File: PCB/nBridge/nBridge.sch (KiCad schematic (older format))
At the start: 23 parts, among them J1 USB_C_Receptacle_USB2.0, J2 Conn_01x06, J3 Conn_01x02, SW1 Switch-SPDT, U1 TPS7A0533PYKAR, U2 BQ25100YFPR, U3 BL652, U4 CC2500Module, U5 M41T62_LC

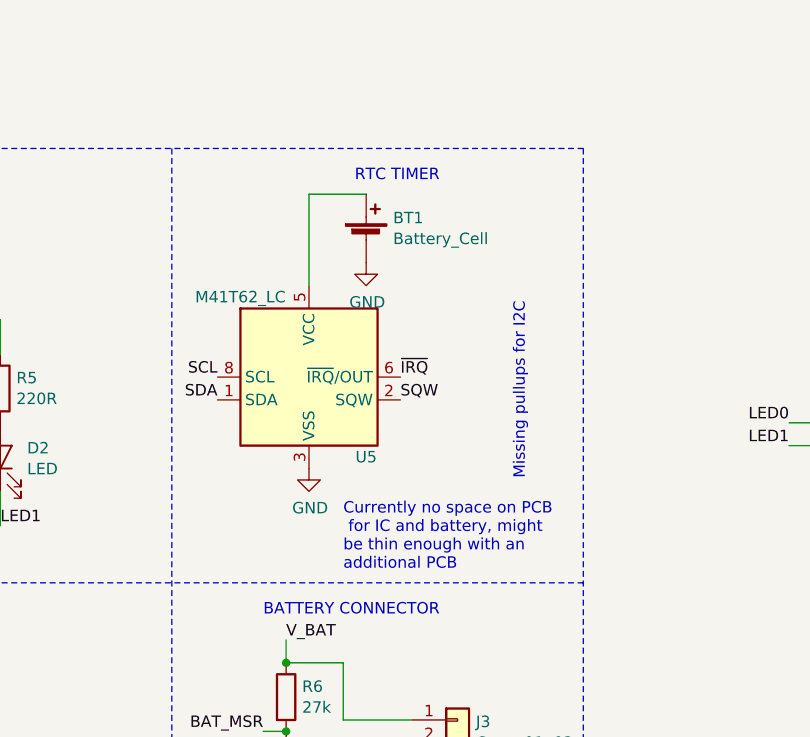
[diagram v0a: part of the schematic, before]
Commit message: Remove RTC
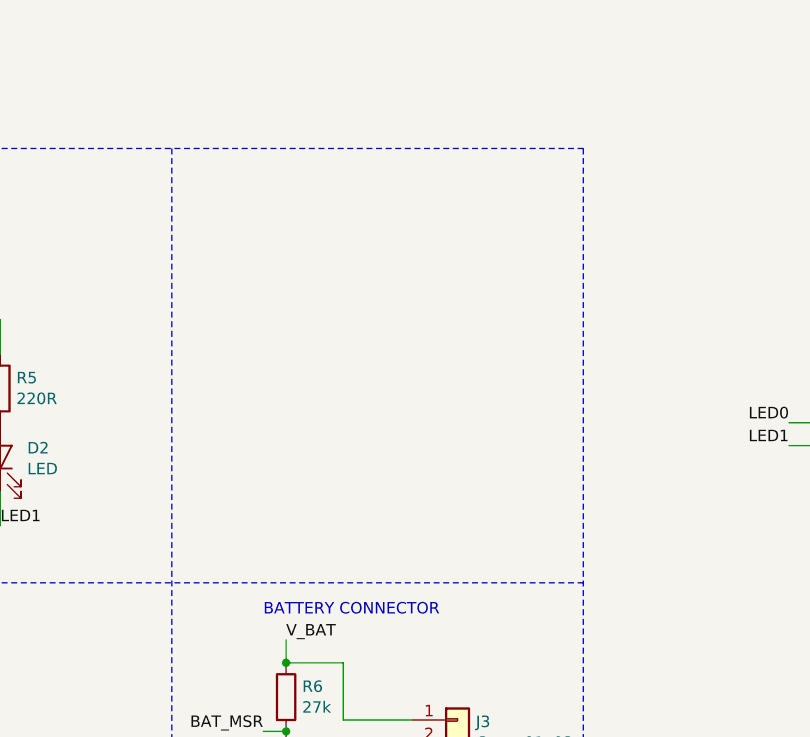
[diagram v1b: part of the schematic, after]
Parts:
- removed BT1: Battery_Cell, symbol Device:Battery_Cell
- removed U5: M41T62_LC, SharedFootprints:M41T62_LLC8_15x32, symbol SharedSymbols:M41T62_LC
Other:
- note removed: "Currently no space on PCB\n for IC and battery, might \nbe thin enough with an \nadditional PCB"
- note removed: "Missing pullups for I2C"
- note removed: "RTC TIMER"
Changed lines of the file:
@@
 Text Notes 1650 1000 0    50   ~ 0
 CC2500 MODULE
-$Comp
-L SharedSymbols:M41T62_LC U5
-U 1 1 5CB38CAA
-P 5750 4150
-F 0 "U5" H 6000 3800 50  0000 C CNN
-F 1 "M41T62_LC" H 5450 4500 50  0000 C CNN
-F 2 "SharedFootprints:M41T62_LLC8_15x32" H 5750 3450 50  0001 C CNN
-F 3 "http://www.st.com/resource/en/datasheet/m41t62.pdf" H 5750 4150 50  0001 C CNN
-	1    5750 4150
-	1    0    0    -1
-$EndComp
-Text Notes 5950 3300 0    50   ~ 0
-RTC TIMER
-$Comp
-L power:GND #PWR017
-U 1 1 5CB3C6E6
-P 5750 4550
-F 0 "#PWR017" H 5750 4300 50  0001 C CNN
-F 1 "GND" H 5755 4377 50  0000 C CNN
-F 2 "" H 5750 4550 50  0001 C CNN
-F 3 "" H 5750 4550 50  0001 C CNN
-	1    5750 4550
-	1    0    0    -1
-$EndComp
-Wire Wire Line
-	5750 3750 5750 3350
-Wire Wire Line
-	5750 3350 6000 3350
-$Comp
-L Device:Battery_Cell BT1
-U 1 1 5CB3FA69
-P 6000 3550
-F 0 "BT1" H 6118 3646 50  0000 L CNN
-F 1 "Battery_Cell" H 6118 3555 50  0000 L CNN
-F 2 "" V 6000 3610 50  0001 C CNN
-F 3 "~" V 6000 3610 50  0001 C CNN
-	1    6000 3550
-	1    0    0    -1
-$EndComp
-$Comp
-L power:GND #PWR018
-U 1 1 5CB4019A
-P 6000 3650
-F 0 "#PWR018" H 6000 3400 50  0001 C CNN
-F 1 "GND" H 6005 3477 50  0000 C CNN
-F 2 "" H 6000 3650 50  0001 C CNN
-F 3 "" H 6000 3650 50  0001 C CNN
-	1    6000 3650
-	1    0    0    -1
-$EndComp
-Text Label 5350 4150 2    50   ~ 0
-SCL
-Text Label 5350 4250 2    50   ~ 0
-SDA
-Text Label 6150 4250 0    50   ~ 0
-SQW
-Text Label 6150 4150 0    50   ~ 0
-~IRQ
-Text Notes 5900 5000 0    50   ~ 0
-Currently no space on PCB\n for IC and battery, might \nbe thin enough with an \nadditional PCB
-Text Notes 6700 4600 1    50   ~ 0
-Missing pullups for I2C
 $EndSCHEMATC

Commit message: Simplify design, fewer and more easily solderable components
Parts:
- removed J1: USB_C_Receptacle_USB2.0, SharedFootprints:12401610E4#2A, symbol Connector:USB_C_Receptacle_USB2.0
- removed R2: 1k35, Resistor_SMD:R_0402_1005Metric, symbol Device:R
- removed R3: 6k, Resistor_SMD:R_0402_1005Metric, symbol Device:R
- removed U1: TPS7A0533PYKAR, SharedFootprints:TPS7A0533PYKAR, symbol SharedSymbols:TPS7A0533PYKAR
- removed U2: BQ25100YFPR, SharedFootprints:BQ25100YFPR, symbol SharedSymbols:BQ25100YFPR
- added J1: 0473460001, digikey-footprints:USB_Micro_B_Female_0473460001, symbol dk_USB-DVI-HDMI-Connectors:0473460001
- added U1: LP5907MFX-3_3_NOPB, digikey-footprints:SOT-753, symbol dk_PMIC-Voltage-Regulators-Linear:LP5907MFX-3_3_NOPB
- added U2: MCP73812T-420I_OT, digikey-footprints:SOT-753, symbol dk_PMIC-Battery-Chargers:MCP73812T-420I_OT
- C1, C2, C3, C4: footprint Capacitor_SMD:C_0402_1005Metric -> Capacitor_SMD:C_0805_2012Metric
- R1: value 10k -> R; footprint Resistor_SMD:R_0402_1005Metric -> Resistor_SMD:R_0805_2012Metric
- R4, R5, R6, R7: footprint Resistor_SMD:R_0402_1005Metric -> Resistor_SMD:R_0805_2012Metric
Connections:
- net +3V3: now also U1.5 (OUT)
- net GND: now also SW1.1 (A), J1.5, J1.SH, U1.2 (GND), U2.2 (VSS); no longer SW1.2 (C)
- net LED0: now also D2.1 (K); no longer D1.1 (K)
- net LED1: now also D1.1 (K); no longer D2.1 (K)
- net V_BAT: now also SW1.2 (C), U1.1 (IN), U2.3 (VBAT); no longer SW1.1 (A)
- net USB+: now reaches C2.1
- net USB+: now also J1.1, U2.1 (CE), U2.4 (VDD)
- net at R1.1: now also U2.5 (PROG)
- net at SW1.3 (B): now also U1.3 (EN)
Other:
- note removed: "(Configured for 100mA fast charge)"
- note removed: "CHARGER\n"
- note removed: "REGULATOR"

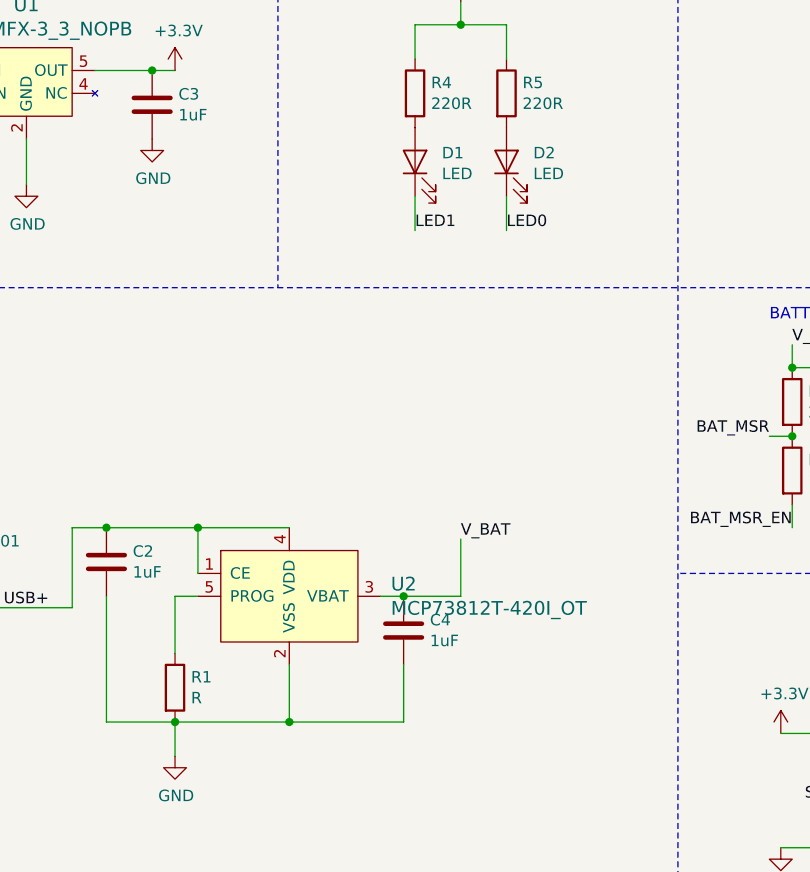
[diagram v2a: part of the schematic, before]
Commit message: Update part values and remove unused silkscreen
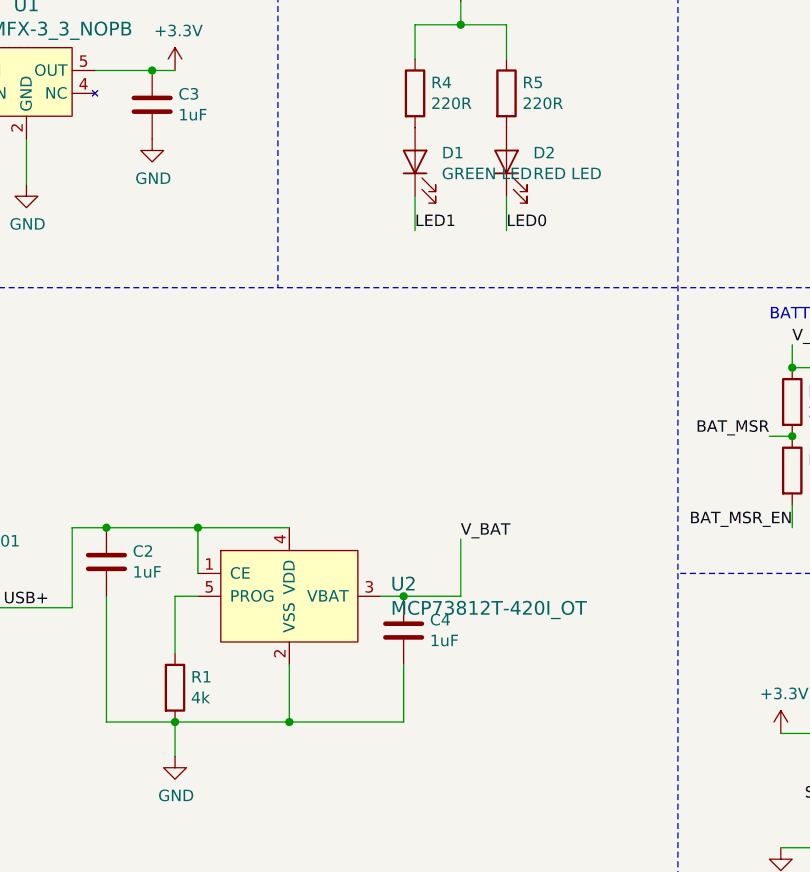
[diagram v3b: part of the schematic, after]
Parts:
- D1: value LED -> GREEN LED
- D2: value LED -> RED LED
- R1: value R -> 4k
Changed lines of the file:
@@
 P 4000 4500
 F 0 "D1" V 4039 4383 50  0000 R CNN
-F 1 "LED" V 3948 4383 50  0000 R CNN
+F 1 "GREEN LED" V 3948 4383 50  0000 R CNN
 F 2 "LED_SMD:LED_0603_1608Metric" H 4000 4500 50  0001 C CNN
 F 3 "~" H 4000 4500 50  0001 C CNN
@@
 P 4400 4500
 F 0 "D2" V 4439 4383 50  0000 R CNN
-F 1 "LED" V 4348 4383 50  0000 R CNN
+F 1 "RED LED" V 4348 4383 50  0000 R CNN
 F 2 "LED_SMD:LED_0603_1608Metric" H 4400 4500 50  0001 C CNN
 F 3 "~" H 4400 4500 50  0001 C CNN
@@
 P 2950 6800
 F 0 "R1" H 3020 6846 50  0000 L CNN
-F 1 "R" H 3020 6755 50  0000 L CNN
+F 1 "4k" H 3020 6755 50  0000 L CNN
 F 2 "Resistor_SMD:R_0805_2012Metric" V 2880 6800 50  0001 C CNN
 F 3 "~" H 2950 6800 50  0001 C CNN
